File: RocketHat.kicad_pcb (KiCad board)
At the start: 2 copper layers, 72.2 x 60.3 mm, 24 parts, among them J1 Screw_Terminal_01x02, J10 Raspberry_Pi_2_3, J2 Conn_01x06_Female, J3 Conn_01x06_Female, J4 Conn_01x07_Female, J5 Conn_01x06_Female, J6 Conn_01x04_Female, J7 Conn_01x10_Female, J8 Conn_01x02, J9 Conn_01x10_Female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

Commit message: Cool Thicc Lines
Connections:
- J10 pad 15: /BNORST -> unconnected-(J10-Pad15)
- J10 pad 18: unconnected-(J10-Pad18) -> /BNORST
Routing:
- net /BNORST: track 0.00 -> 53.0 mm
- net /SENSOR_SDA: track 110.6 -> 60.8 mm
- net /SENSOR_SCL: track 113.7 -> 65.0 mm
- net /EEPROM_SDA: track 26.3 -> 5.04 mm
- net /EEPROM_SCL: track 22.5 -> 5.66 mm
- net /3V3: track 250.4 -> 258.9 mm
- net /XBEE_TX: track 37.6 -> 36.1 mm
- net /P5V_HAT: track 45.0 -> 46.4 mm

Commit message: Fixed DRC
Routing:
- net /EEPROM_SDA: track 5.04 -> 56.1 mm
- net /SENSOR_SDA: track 60.8 -> 111.7 mm
- net /SENSOR_SCL: track 65.0 -> 113.4 mm
- net /EEPROM_SCL: track 5.66 -> 50.8 mm
- net /3V3: track 258.9 -> 262.8 mm

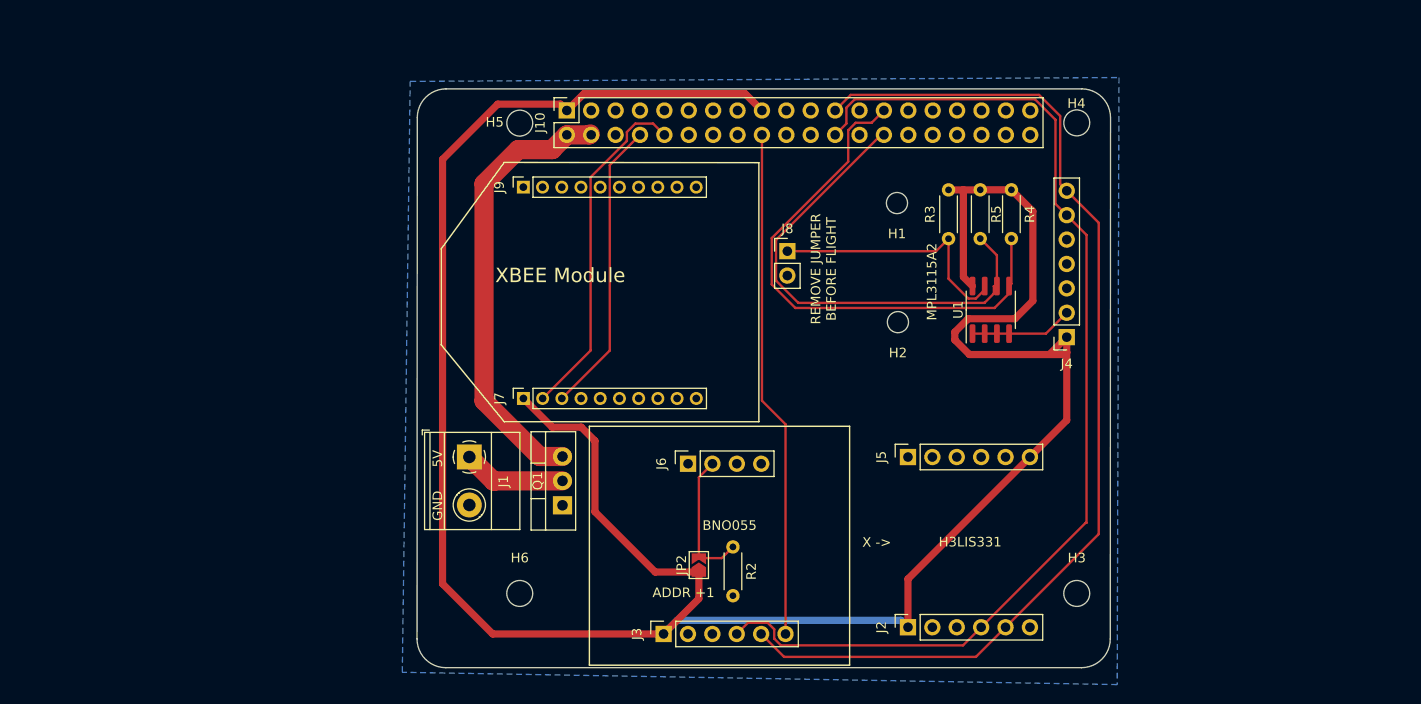
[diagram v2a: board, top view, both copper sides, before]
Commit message: Fixed Inverted Layout
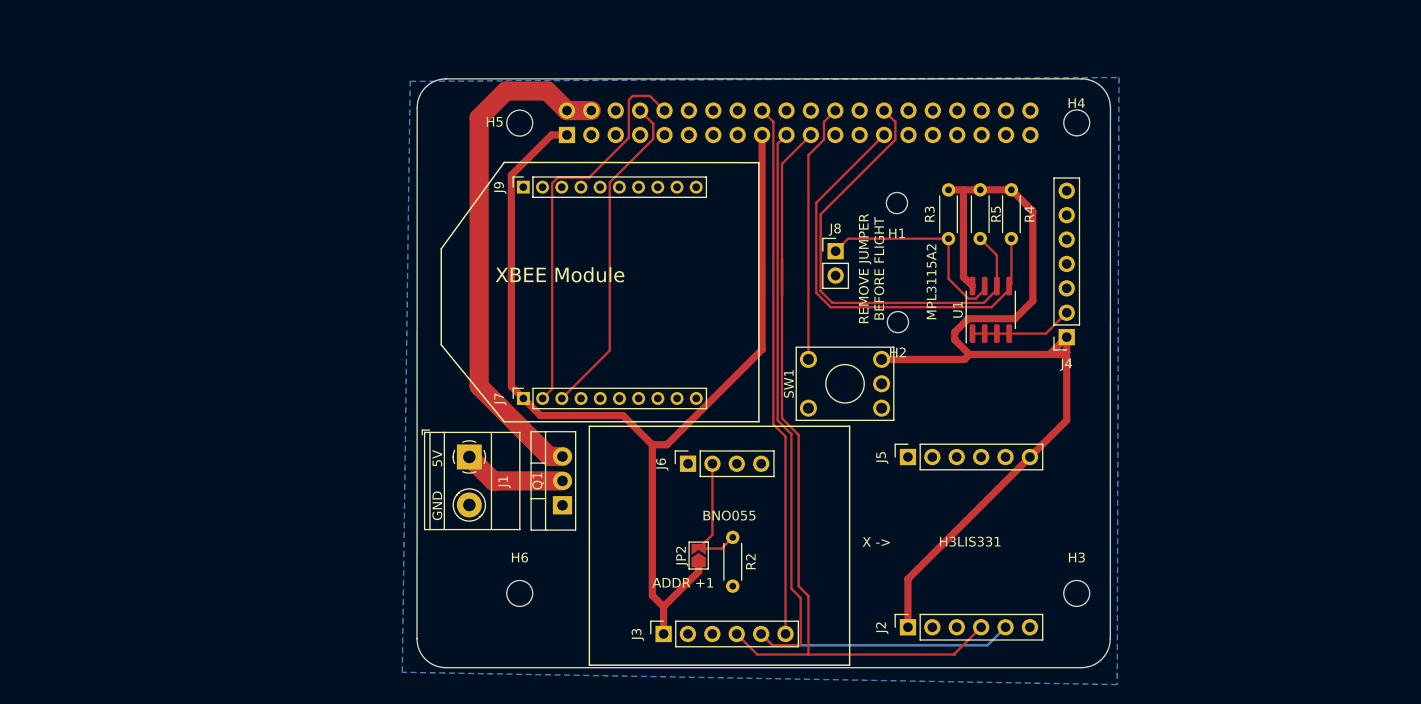
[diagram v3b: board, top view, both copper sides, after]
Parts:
- added SW1: SW_Reed_SPDT, Button_Switch_THT:KSA_Tactile_SPST, F.Cu at (123.2, 59.9)
- J10: moved to B.Cu
- moved J8 5.03 mm to (126.0, 43.6)
- moved J10 2.55 mm to (98.0, 31.5), turned to -90 degrees
- moved JP2 0.99 mm to (111.8, 75.3)
- moved R2 0.99 mm to (115.3, 73.4)
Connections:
- J10 pad 19: unconnected-(J10-Pad19) -> /IMU_SDA
- J10 pad 21: unconnected-(J10-Pad21) -> /IMU_SCL
- J10 pad 23: /SENSOR_SDA -> unconnected-(J10-Pad23)
- J10 pad 24: /SENSOR_SCL -> /WIFI_EN
- J10 pad 38: unconnected-(J10-Pad38) -> /ALT_SCL
- J10 pad 40: unconnected-(J10-Pad40) -> /ALT_SDA
- J2 pad 4: /SENSOR_SCL -> /IMU_SCL
- J2 pad 5: /SENSOR_SDA -> /IMU_SDA
- J3 pad 4: /SENSOR_SCL -> /IMU_SCL
- J3 pad 5: /SENSOR_SDA -> /IMU_SDA
- J4 pad 6: /SENSOR_SCL -> /ALT_SCL
- J4 pad 7: /SENSOR_SDA -> /ALT_SDA
- J7 pad 2: /XBEE_TX -> /XBEE_RX
- J7 pad 3: /XBEE_RX -> /XBEE_TX
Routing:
- net /SENSOR_SCL: track 113.4 -> 0.00 mm
- net /SENSOR_SDA: track 111.7 -> 0.00 mm
- net /IMU_SCL: track 0.00 -> 87.9 mm
- net /IMU_SDA: track 0.00 -> 85.8 mm
- net /3V3: track 262.8 -> 212.0 mm
- net /WIFI_EN: track 0.00 -> 27.1 mm
- net /EEPROM_SDA: track 56.1 -> 46.2 mm
- net /P5V_HAT: track 46.4 -> 53.3 mm
- net /XBEE_TX: track 36.1 -> 41.2 mm
- net Net-(J8-Pad1): track 26.5 -> 21.5 mm
- net /XBEE_RX: track 30.8 -> 34.5 mm
- net /EEPROM_SCL: track 50.8 -> 48.0 mm
- net /BNORST: track 53.0 -> 55.5 mm
- net /ADR_BNO055: track 14.4 -> 13.5 mm
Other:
- board size 72.2 x 60.3 mm -> 72.2 x 61.3 mm

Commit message: Passed DRC With 1.1.1
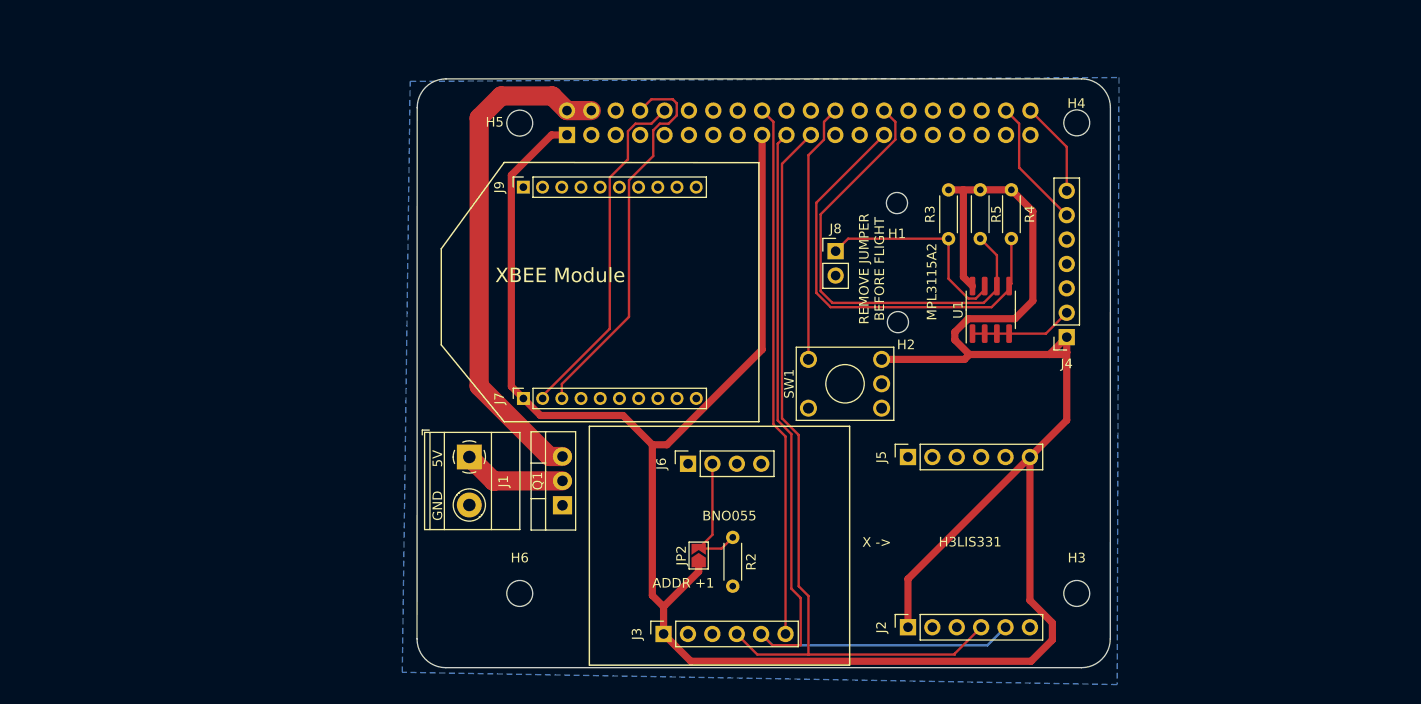
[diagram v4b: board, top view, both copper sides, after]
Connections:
- J10 pad 10: /XBEE_TX -> /PI_RX
- J10 pad 8: /XBEE_RX -> /PI_TX
- J7 pad 2: /XBEE_RX -> /PI_RX
- J7 pad 3: /XBEE_TX -> /PI_TX
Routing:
- net /3V3: track 212.0 -> 274.6 mm
- net /XBEE_TX: track 41.2 -> 0.00 mm
- net /PI_TX: track 0.00 -> 40.7 mm
- net /PI_RX: track 0.00 -> 36.2 mm
- net /XBEE_RX: track 34.5 -> 0.00 mm
- net /ALT_SCL: track 0.00 -> 13.5 mm
- net /ALT_SDA: track 0.00 -> 9.92 mm
- net /IMU_SCL: track 87.9 -> 84.1 mm

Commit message: Updated Schematics and Footprints
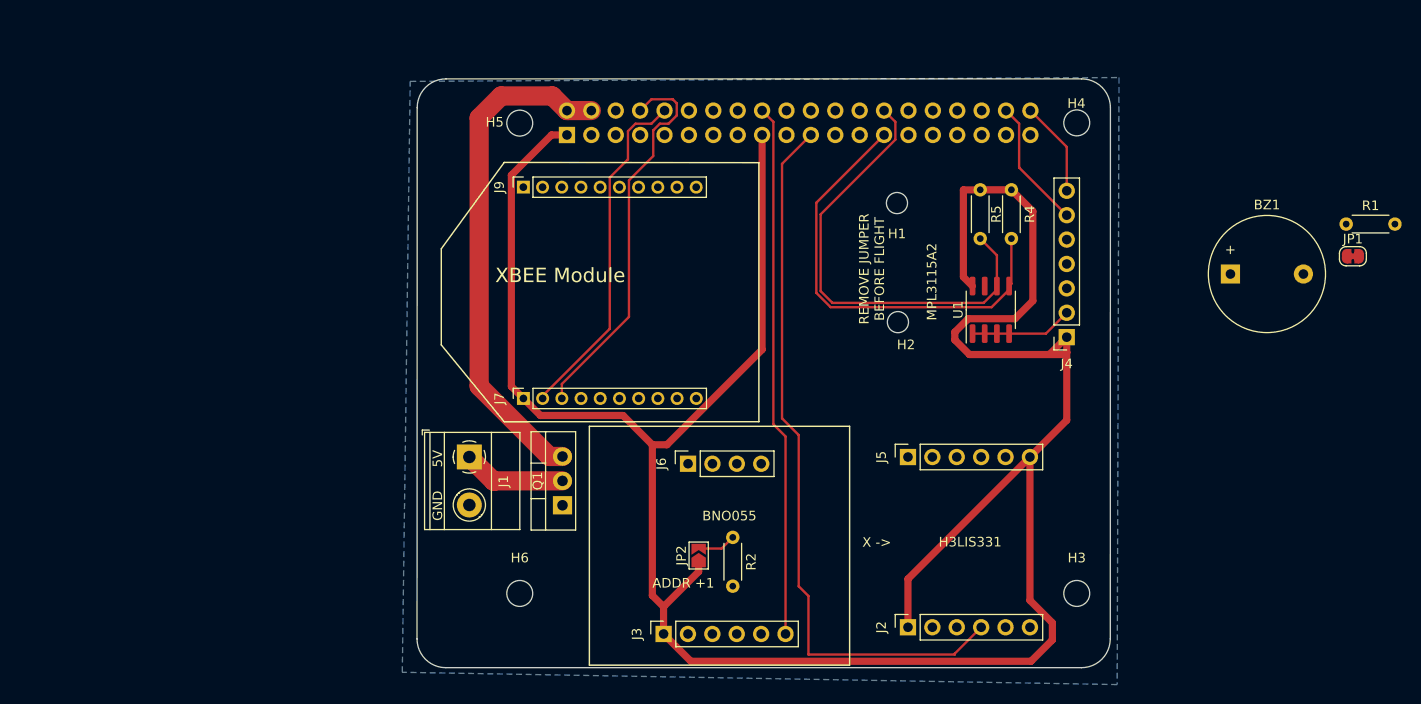
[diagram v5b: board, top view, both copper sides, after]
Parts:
- removed J8: Conn_01x02, Connector_PinHeader_2.54mm:PinHeader_1x02_P2.54mm_Vertical
- removed R3: 10K 1%, Resistor_THT:R_Axial_DIN0204_L3.6mm_D1.6mm_P5.08mm_Horizontal
- removed SW1: SW_Reed_SPDT, Button_Switch_THT:KSA_Tactile_SPST
- added BZ1: Buzzer, Buzzer_Beeper:Buzzer_12x9.5RM7.6, F.Cu at (167.1, 46.0)
- added JP1: SolderJumper_2_Bridged, Jumper:SolderJumper-2_P1.3mm_Bridged_RoundedPad1.0x1.5mm, F.Cu at (179.9, 44.1)
- added R1: 10k, Resistor_THT:R_Axial_DIN0204_L3.6mm_D1.6mm_P5.08mm_Horizontal, F.Cu at (179.2, 40.8)
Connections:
- J10 pad 12: unconnected-(J10-Pad12) -> /BUZ
- J10 pad 24: /WIFI_EN -> unconnected-(J10-Pad24)
- J3 pad 4: /IMU_SCL -> /IMU_SDA
- J3 pad 5: /IMU_SDA -> /IMU_SCL
- J6 pad 2: /ADR_BNO055 -> unconnected-(J6-Pad2)
- J6 pad 4: unconnected-(J6-Pad4) -> /ADR_BNO055
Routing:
- net /IMU_SDA: track 85.8 -> 0.00 mm
- net /WIFI_EN: track 27.1 -> 0.00 mm
- net Net-(JP1-Pad2): track 21.5 -> 0.00 mm
- net /3V3: track 274.6 -> 263.7 mm
- net /ADR_BNO055: track 13.5 -> 4.03 mm
- net /IMU_SCL: track 84.1 -> 75.7 mm

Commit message: Added Mounting Holes for all sensors
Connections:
- J4 pad 6: /ALT_SCL -> /IMU_SCL
- J4 pad 7: /ALT_SDA -> /IMU_SDA
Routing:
- net /BNORST: track 55.5 -> 0.00 mm
- net /IMU_SCL: track 75.7 -> 25.0 mm
- net /ALT_SCL: track 13.5 -> 0.00 mm
- net /ALT_SDA: track 9.92 -> 0.00 mm
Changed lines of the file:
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@@
       (net 39 "unconnected-(J4-Pad5)") (pinfunction "Pin_5") (pintype "passive+no_connect"))
     (pad "6" thru_hole oval locked (at 0 12.7 180) (size 1.7 1.7) (drill 1) (layers *.Cu *.Mask)
-      (net 57 "/ALT_SCL") (pinfunction "Pin_6") (pintype "passive"))
+      (net 58 "/IMU_SCL") (pinfunction "Pin_6") (pintype "passive"))
     (pad "7" thru_hole oval locked (at 0 15.24 180) (size 1.7 1.7) (drill 1) (layers *.Cu *.Mask)
-      (net 56 "/ALT_SDA") (pinfunction "Pin_7") (pintype "passive"))
+      (net 59 "/IMU_SDA") (pinfunction "Pin_7") (pintype "passive"))
     (model "${KICAD6_3DMODEL_DIR}/Connector_PinSocket_2.54mm.3dshapes/PinSocket_1x07_P2.54mm_Vertical.wrl"
       (offset (xyz 0 0 0))
@@
   (segment (start 110.945119 86.297519) (end 108.103 83.4554) (width 0.75) (layer "F.Cu") (net 5))
   (segment (start 148.2772 54.356) (end 150.0854 52.5478) (width 0.75) (layer "F.Cu") (net 5))
-  (segment (start 118.364 28.956) (end 119.538511 30.130511) (width 0.25) (layer "F.Cu") (net 8))
-  (segment (start 119.538511 30.130511) (end 119.538511 61.626511) (width 0.25) (layer "F.Cu") (net 8))
-  (segment (start 119.538511 61.626511) (end 120.803 62.891) (width 0.25) (layer "F.Cu") (net 8))
-  (segment (start 120.803 62.891) (end 120.803 83.4554) (width 0.25) (layer "F.Cu") (net 8))
   (segment (start 124.01048 47.938197) (end 124.01048 38.54952) (width 0.25) (layer "F.Cu") (net 19))
   (segment (start 124.01048 38.54952) (end 131.064 31.496) (width 0.25) (layer "F.Cu") (net 19))
@@
   (segment (start 142.813 44.0202) (end 142.813 47.2304) (width 0.25) (layer "F.Cu") (net 20))
   (segment (start 124.46 47.752) (end 125.68744 48.97944) (width 0.25) (layer "F.Cu") (net 20))
-  (segment (start 150.0854 32.7374) (end 146.304 28.956) (width 0.25) (layer "F.Cu") (net 56))
-  (segment (start 150.0854 37.3078) (end 150.0854 32.7374) (width 0.25) (layer "F.Cu") (net 56))
-  (segment (start 143.764 28.956) (end 145.129489 30.321489) (width 0.25) (layer "F.Cu") (net 57))
-  (segment (start 145.129489 30.321489) (end 145.129489 34.891889) (width 0.25) (layer "F.Cu") (net 57))
-  (segment (start 145.129489 34.891889) (end 150.0854 39.8478) (width 0.25) (layer "F.Cu") (net 57))
-  (segment (start 123.19 79.502) (end 123.19 85.598) (width 0.25) (layer "F.Cu") (net 58))
-  (segment (start 122.174 78.486) (end 123.19 79.502) (width 0.25) (layer "F.Cu") (net 58))
-  (segment (start 123.444 31.496) (end 120.437551 34.502449) (width 0.25) (layer "F.Cu") (net 58))
+  (segment (start 120.4056 85.598) (end 138.43 85.598) (width 0.25) (layer "F.Cu") (net 58))
+  (segment (start 118.263 83.4554) (end 120.4056 85.598) (width 0.25) (layer "F.Cu") (net 58))
   (segment (start 138.43 85.598) (end 138.43 85.4984) (width 0.25) (layer "F.Cu") (net 58))
-  (segment (start 123.19 85.598) (end 138.43 85.598) (width 0.25) (layer "F.Cu") (net 58))
-  (segment (start 122.174 62.738) (end 122.174 78.486) (width 0.25) (layer "F.Cu") (net 58))
-  (segment (start 120.437551 61.001551) (end 122.174 62.738) (width 0.25) (layer "F.Cu") (net 58))
-  (segment (start 120.437551 34.502449) (end 120.437551 61.001551) (width 0.25) (layer "F.Cu") (net 58))
   (segment (start 138.43 85.4984) (end 141.173 82.7554) (width 0.25) (layer "F.Cu") (net 58))
   (segment (start 102.503489 51.674511) (end 95.5106 58.6674) (width 0.25) (layer "F.Cu") (net 61))
@@
     (connect_pads (clearance 0.508))
     (min_thickness 0.254) (filled_areas_thickness no)
-    (fill yes (thermal_gap 0.508) (thermal_bridge_width 0.508))
+    (fill (thermal_gap 0.508) (thermal_bridge_width 0.508))
     (polygon
       (pts
         (xy 155.338 88.7254)
         (xy 80.898 87.4454)
-        (xy 81.718 25.9154)
-        (xy 155.528 25.5154)
+        (xy 81.68508 19.840867)
+        (xy 155.49508 19.440867)
       )
     )

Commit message: Cleared Layout
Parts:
- removed the J9 at (93.5, 36.9)
- removed R5: 3.9K, Resistor_THT:R_Axial_DIN0204_L3.6mm_D1.6mm_P5.08mm_Horizontal
- added H3: MountingHole, MountingHole:MountingHole_2.2mm_M2, F.Cu at (51.9, 40.4)
- added H4: MountingHole, MountingHole:MountingHole_2.2mm_M2, F.Cu at (61.0, 44.4)
- added H5: MountingHole, MountingHole:MountingHole_2.2mm_M2, F.Cu at (73.0, 57.7)
- added H6: MountingHole, MountingHole:MountingHole_2.2mm_M2, F.Cu at (67.0, 51.7)
- added J8: Conn_01x10_Female, Connector_PinSocket_2.00mm:PinSocket_1x10_P2.00mm_Vertical, F.Cu at (44.5, 79.3)
- added R3: 3.9K, Resistor_THT:R_Axial_DIN0204_L3.6mm_D1.6mm_P5.08mm_Horizontal, F.Cu at (72.4, 83.9)
- BZ1: footprint Buzzer_Beeper:Buzzer_12x9.5RM7.6 -> Buzzer_Beeper:Buzzer_TDK_PS1240P02BT_D12.2mm_H6.5mm
- J4: value Conn_01x07_Female -> Conn_01x06_Female; footprint Connector_PinSocket_2.54mm:PinSocket_1x07_P2.54mm_Vertical -> Connector_PinSocket_2.54mm:PinSocket_1x06_P2.54mm_Vertical
- J5: value Conn_01x06_Female -> Conn_01x04_Female; footprint Connector_PinSocket_2.54mm:PinSocket_1x06_P2.54mm_Vertical -> Connector_PinSocket_2.54mm:PinSocket_1x04_P2.54mm_Vertical
- J6: value Conn_01x04_Female -> Conn_01x07_Female; footprint Connector_PinSocket_2.54mm:PinSocket_1x04_P2.54mm_Vertical -> Connector_PinSocket_2.54mm:PinSocket_1x07_P2.54mm_Vertical
- JP1: value SolderJumper_2_Bridged -> SolderJumper_2_Open; footprint Jumper:SolderJumper-2_P1.3mm_Bridged_RoundedPad1.0x1.5mm -> Jumper:SolderJumper-2_P1.3mm_Open_TrianglePad1.0x1.5mm
- JP2: value SolderJumper_2_Open -> SolderJumper_2_Bridged; footprint Jumper:SolderJumper-2_P1.3mm_Open_TrianglePad1.0x1.5mm -> Jumper:SolderJumper-2_P1.3mm_Bridged_RoundedPad1.0x1.5mm
- R1: value 10k -> 10K
- R2: value 10K -> 10k
- moved R1 118.1 mm to (69.3, 83.9), turned to 90 degrees
- moved BZ1 117.1 mm to (50.3, 54.2), turned to 90 degrees
- moved JP1 114.1 mm to (65.8, 45.2), turned to 90 degrees
- moved J4 106.7 mm to (44.8, 70.4), turned to 90 degrees
- moved U1 97.0 mm to (45.7, 39.1)
- moved J2 90.3 mm to (44.8, 65.8)
- moved H1 87.2 mm to (45.5, 31.9), turned to 90 degrees
- moved R4 78.8 mm to (73.3, 71.2), turned to 90 degrees
- moved JP2 73.0 mm to (50.7, 35.2)
- moved J5 69.6 mm to (64.7, 75.0)
- moved J3 67.1 mm to (44.8, 61.2)
- moved J6 66.5 mm to (44.8, 75.0)
- moved H2 65.8 mm to (67.0, 57.7), turned to 90 degrees
- moved J7 54.7 mm to (44.5, 83.4)
- moved R2 50.3 mm to (66.1, 83.9), turned to 90 degrees
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- renumbered H6 to H10, H3 to H7, H4 to H8, H5 to H9, J10 to J9
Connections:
- J3 pad 1: /3V3 -> unconnected-(J3-Pad1)
- J3 pad 3: GND -> unconnected-(J3-Pad3)
- J3 pad 4: /IMU_SDA -> unconnected-(J3-Pad4)
- J3 pad 5: /IMU_SCL -> unconnected-(J3-Pad5)
- J3 pad 6: /BNORST -> /3V3
- J4 pad 2: GND -> unconnected-(J4-Pad2)
- J4 pad 3: unconnected-(J4-Pad3) -> GND
- J4 pad 4: unconnected-(J4-Pad4) -> /IMU_SDA
- J4 pad 5: unconnected-(J4-Pad5) -> /IMU_SCL
- J4 pad 6: /IMU_SCL -> /BNORST
- J5 pad 4: unconnected-(J5-Pad4) -> /ADR_BNO055
- J6 pad 1: unconnected-(J6-Pad1) -> /3V3
- J6 pad 2: unconnected-(J6-Pad2) -> GND
- J6 pad 4: /ADR_BNO055 -> unconnected-(J6-Pad4)
- J9 pad 38: /ALT_SCL -> unconnected-(J9-Pad38)
- J9 pad 40: /ALT_SDA -> unconnected-(J9-Pad40)
- JP1 pad 2: Net-(JP1-Pad2) -> /ADR_BNO055
- JP2 pad 2: /ADR_BNO055 -> Net-(JP2-Pad2)
- R1 pad 1: GND -> /ADR_BNO055
- R1 pad 2: Net-(JP1-Pad2) -> GND
- R2 pad 1: /ADR_BNO055 -> GND
- R2 pad 2: GND -> Net-(JP2-Pad2)
- R4 pad 2: /EEPROM_SDA -> /EEPROM_SCL
- U1 pad 7: Net-(JP1-Pad2) -> Net-(JP2-Pad2)
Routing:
- net /3V3: track 263.7 -> 0.00 mm
- net /P5V_HAT: track 52.9 -> 2.54 mm
- net /EEPROM_SCL: track 47.6 -> 0.00 mm
- net /EEPROM_SDA: track 45.9 -> 0.00 mm
- net /PI_TX: track 40.7 -> 0.00 mm
- net /PI_RX: track 35.9 -> 0.00 mm
- net /IMU_SCL: track 25.0 -> 0.00 mm
- net Net-(J1-Pad1): track 10.8 -> 0.00 mm
- net GND: track 10.7 -> 0.00 mm
- net /ADR_BNO055: track 4.03 -> 0.00 mm
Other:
- board text added: "By Jacob Armstrong"
- board text removed: "5V"
- board text removed: "ADDR +1"
- board text removed: "BNO055"
- board text removed: "GND"
- board text removed: "H3LIS331"
- board text removed: "MPL3115A2"
- board text removed: "REMOVE JUMPER BEFORE FLIGHT"
- board text removed: "X ->"
- board text removed: "XBEE Module"
